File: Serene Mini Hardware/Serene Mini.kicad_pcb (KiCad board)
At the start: 6 copper layers, 35 x 60.5 mm, 52 parts, among them J1 USB_C_Receptacle, J2 Conn_01x04_Pin, U1 AP7361C-33E, U2 AP2112K-1.8, U3 STM32H753ZITx, U4 ADXL382-1BCCZ-RL, U5 ADAU1787BCBZRL, Y1 Crystal_GND24, Y2 32.768 kHz

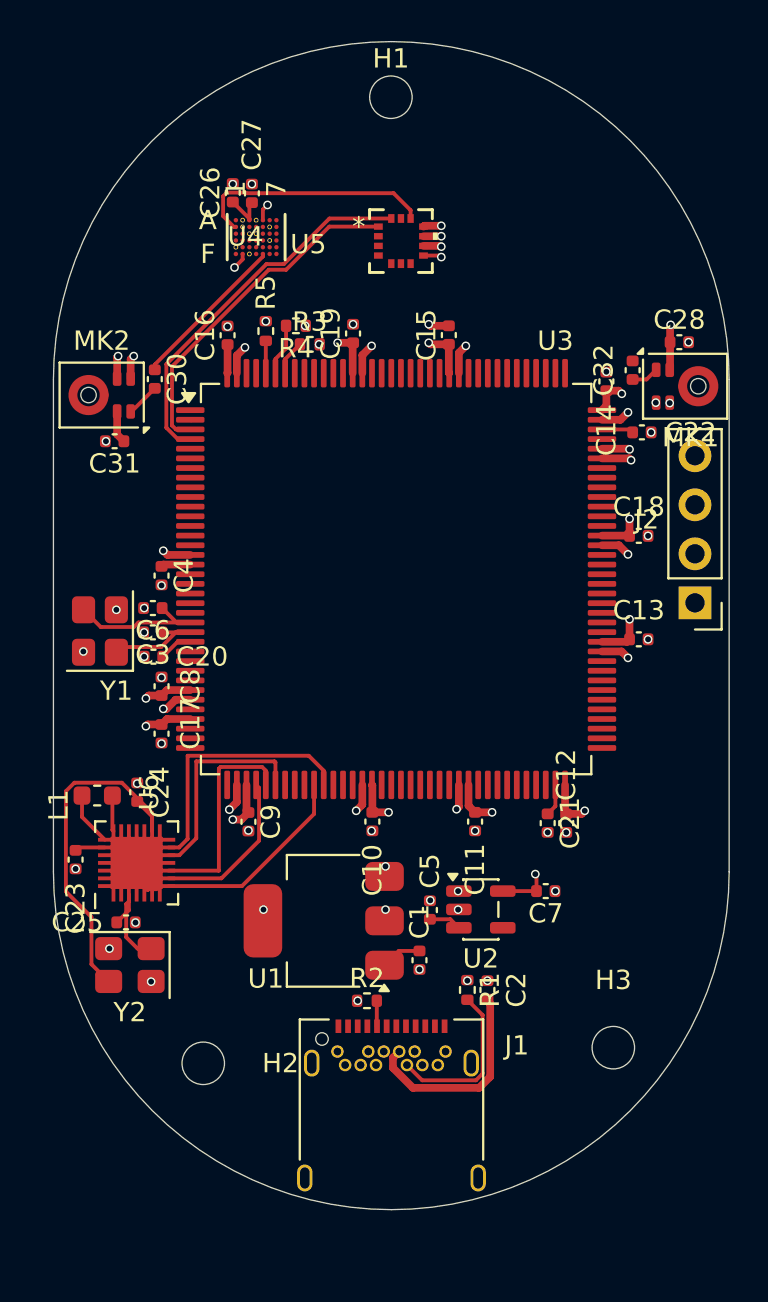
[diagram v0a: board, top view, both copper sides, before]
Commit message: PCB and Schematic Design Changes
Upgraded to the newer sr1120
Reduced the PCB size by ~40%
More efficient layout with chips on both side of the pcb
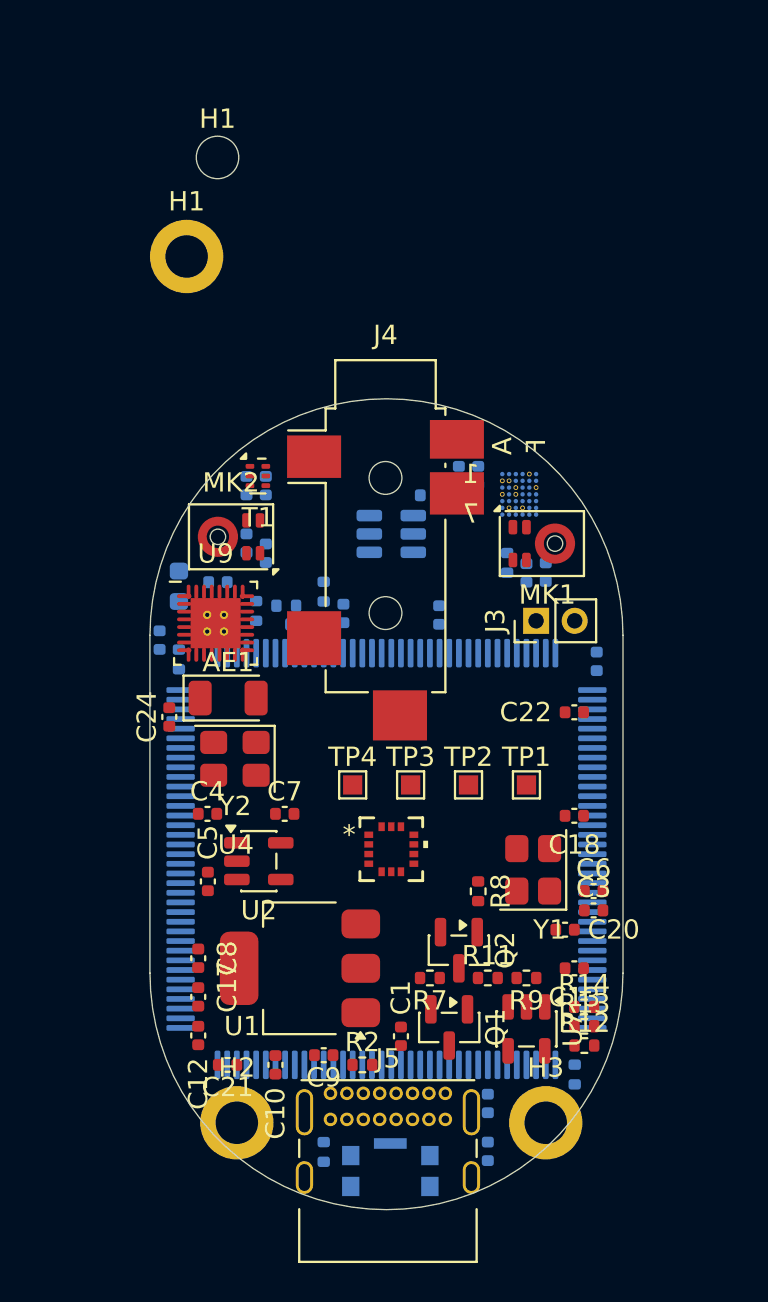
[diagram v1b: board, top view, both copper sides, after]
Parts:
- removed the H1 at (33.5, 20.9)
- removed J1: USB_C_Receptacle, Connector_USB:USB_C_Receptacle_Amphenol_12401548E4-2A
- removed J2: Conn_01x04_Pin, Connector_PinHeader_2.54mm:PinHeader_1x04_P2.54mm_Vertical
- removed U6: ~, ANC_Parts:Spark_SR1020_QFN28
- added AE1: Antenna_Chip, RF_Antenna:Johanson_2450AT18x100, F.Cu at (25.1, 52.0)
- added C29: 1uF, Capacitor_SMD:C_0402_1005Metric, B.Cu at (35.5, 41.5)
- added C33: 10pF, Capacitor_SMD:C_0402_1005Metric, B.Cu at (26.0, 41.0)
- added C34: 10pF, Capacitor_SMD:C_0402_1005Metric, B.Cu at (27.0, 41.0)
- added H1: MountingHole, MountingHole:MountingHole_2.2mm_M2_DIN965_Pad, F.Cu at (22.9, 29.1)
- added H1: MountingHole, MountingHole:MountingHole_2.2mm_M2, F.Cu at (24.5, 24.0)
- added J3: Conn_01x02, Connector_PinHeader_2.00mm:PinHeader_1x02_P2.00mm_Vertical, F.Cu at (41.0, 48.0)
- added J4: AudioJack3_Switch, Connector_Audio:Jack_3.5mm_CUI_SJ2-3593D-SMT_Horizontal, F.Cu at (33.2, 43.1)
- added J5: USB_C_Receptacle_USB2.0_14P, Connector_USB:USB_C_Receptacle_GCT_USB4085, F.Cu at (30.4, 72.5)
- added Q1: Q_PMOS_GSD, Package_TO_SOT_SMD:SOT-23, F.Cu at (36.5, 69.1)
- added Q2: Q_NPN_BCE, Package_TO_SOT_SMD:SOT-23, F.Cu at (37.0, 65.1)
- added R10: 100kΩ, Resistor_SMD:R_0402_1005Metric, B.Cu at (39.5, 45.0)
- added R11: 100kΩ, Resistor_SMD:R_0402_1005Metric, F.Cu at (38.5, 66.5)
- added R12: 220Ω, Resistor_SMD:R_0402_1005Metric, F.Cu at (43.5, 70.0)
- added R13: 100Ω, Resistor_SMD:R_0402_1005Metric, F.Cu at (43.5, 69.0)
- added R14: 100Ω, Resistor_SMD:R_0402_1005Metric, F.Cu at (43.5, 68.0)
- added R15: 10kΩ, Resistor_SMD:R_0402_1005Metric, B.Cu at (30.0, 46.5)
- added R16: 100kΩ, Resistor_SMD:R_0402_1005Metric, B.Cu at (22.5, 50.0)
- added R6: 2kΩ, Resistor_SMD:R_0402_1005Metric, B.Cu at (43.0, 71.5)
- added R7: 100kΩ, Resistor_SMD:R_0402_1005Metric, F.Cu at (35.5, 66.5)
- added R8: 10kΩ, Resistor_SMD:R_0402_1005Metric, F.Cu at (38.0, 62.0)
- added R9: 100kΩ, Resistor_SMD:R_0402_1005Metric, F.Cu at (40.5, 66.5)
- added SW1: SW_Push, Button_Switch_SMD:SW_Push_1P1T-SH_NO_CK_KMR2xxG, B.Cu at (33.5, 76.5)
- added T1: Transformer_1P_1S, RF_Converter:Balun_Johanson_1.6x0.8mm, F.Cu at (26.6, 40.5)
- added TP1: TestPoint, TestPoint:TestPoint_Pad_1.0x1.0mm, F.Cu at (40.5, 56.5)
- added TP2: TestPoint, TestPoint:TestPoint_Pad_1.0x1.0mm, F.Cu at (37.5, 56.5)
- added TP3: TestPoint, TestPoint:TestPoint_Pad_1.0x1.0mm, F.Cu at (34.5, 56.5)
- added TP4: TestPoint, TestPoint:TestPoint_Pad_1.0x1.0mm, F.Cu at (31.5, 56.5)
- added U7: MCP73831-2-OT, Package_TO_SOT_SMD:SOT-23-5, F.Cu at (40.5, 69.1)
- added U8: USBLC6-2SC6, Package_TO_SOT_SMD:SOT-23-6, B.Cu at (33.5, 43.5)
- added U9: ~, ANC_Parts:Spark_SR1120_QFN32, F.Cu at (24.4, 48.1)
- C11, C14, C15, C16, C19, C2, C23, C25, C26, C27, C28, C30, C31, C32, L1, R1, R3, R4, R5, U3, U5: moved to B.Cu
- H2, H3: footprint MountingHole:MountingHole_2.2mm_M2 -> MountingHole:MountingHole_2.2mm_M2_DIN965_Pad
- moved U4 31.5 mm to (33.5, 59.8)
- moved C6 27.1 mm to (44.0, 62.0), turned to 0 degrees
- moved C3 27.0 mm to (44.0, 63.0), turned to 0 degrees
- moved Y1 25.6 mm to (40.9, 60.9)
- moved C20 25.6 mm to (42.5, 64.0)
- moved C12 22.0 mm to (23.5, 69.5), turned to 90 degrees
- moved C21 20.8 mm to (25.0, 71.0), turned to 180 degrees
- moved C26 19.4 mm to (38.0, 40.5), turned to -90 degrees
- moved U5 19.1 mm to (40.1, 41.5), turned to -90 degrees
- moved C25 18.3 mm to (24.5, 46.0)
- moved C27 18.1 mm to (37.0, 40.5), turned to -90 degrees
- moved C13 17.4 mm to (43.0, 66.0), turned to 180 degrees
- moved C11 17.1 mm to (38.5, 75.5)
- moved C22 14.9 mm to (43.0, 52.7), turned to 180 degrees
- moved C18 14.9 mm to (43.0, 58.1), turned to 180 degrees
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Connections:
- C23 pad 1: Net-(U6-AVDD_1V) -> Net-(U9-VDD_IO)
- L1 pad 1: Net-(U6-AVDD_1V) -> Net-(U9-VDD_CORE_ANA)
- U3 pad 115: unconnected-(U3-PD1-Pad115) -> /HP_DETECT
- U3 pad 133: unconnected-(U3-PB3-Pad133) -> /UWB_SHDN
- U3 pad 34: unconnected-(U3-PA0-Pad34) -> /<NO NET>
- U3 pad 35: unconnected-(U3-PA1-Pad35) -> /CHG_STAT
- U3 pad 81: unconnected-(U3-PD12-Pad81) -> /PWR_HOLD
- U3 pad 82: unconnected-(U3-PD13-Pad82) -> /LED_R
- U3 pad 85: unconnected-(U3-PD14-Pad85) -> /LED_G
- U3 pad 86: unconnected-(U3-PD15-Pad86) -> /LED_B
- U5 pad E1: GND -> +1V8
- U5 pad E2: unconnected-(U5-HPOUTP0/LOUTP0-PadE2) -> /HPOUTR
- U5 pad F1: unconnected-(U5-HPOUTN0/LOUTP0-PadF1) -> /HPOUTL
- U5 pad F2: +1V8 -> +3.3V
- U5 pad F4: unconnected-(U5-CM-PadF4) -> +1V8
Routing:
- net +3.3V: track 49.9 -> 0.00 mm, vias 21 -> 0
- net GND: track 21.2 -> 0.00 mm, vias 53 -> 0
- net Net-(U9-XTAL_C2): track 19.6 -> 0.00 mm
- net /SAI_BCLK: track 19.5 -> 0.00 mm
- net /SAI_FS: track 17.8 -> 0.00 mm
- net /UWB_RST: track 13.6 -> 0.00 mm
- net /VIB_DATA: track 12.5 -> 0.00 mm
- net /UWB_SCK: track 11.2 -> 0.00 mm
- net /UWB_MISO: track 11.1 -> 0.00 mm
- net /UWB_IRQ: track 10.6 -> 0.00 mm
- net Net-(J5-CC2): track 8.54 -> 0.00 mm
- net /UWB_CS: track 8.45 -> 0.00 mm
- net /MIC2: track 8.32 -> 0.00 mm
- net Net-(U3-PH0): track 7.76 -> 0.00 mm
- net Net-(U3-PH1): track 5.72 -> 0.00 mm
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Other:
- board size 35 x 60.5 mm -> 24.5 x 42 mm

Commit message: Final PCB and Schematic Design
- Added new IC to support fast charging for batteries up to 3000mAh

- Added a bluetooth chip

- Used smaller coaxial ports to increase available space

- The button is now located off the board connected via molax

- Finished routing
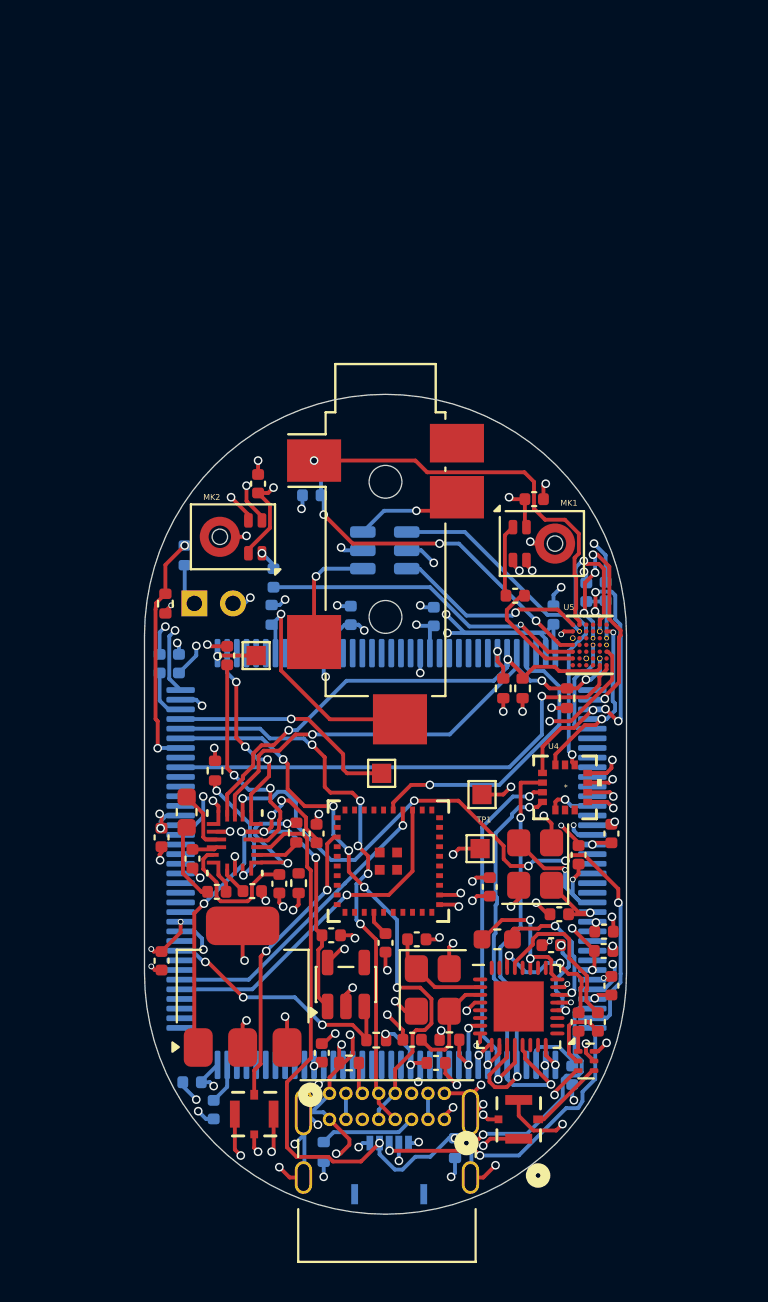
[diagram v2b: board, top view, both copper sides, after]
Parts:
- removed AE1: Antenna_Chip, RF_Antenna:Johanson_2450AT18x100
- removed C5: 10uF, Capacitor_SMD:C_0402_1005Metric
- removed H1, H2, H3: MountingHole, MountingHole:MountingHole_2.2mm_M2_DIN965_Pad
- removed H1: MountingHole, MountingHole:MountingHole_2.2mm_M2
- removed Q1: Q_PMOS_GSD, Package_TO_SOT_SMD:SOT-23
- removed Q2: Q_NPN_BCE, Package_TO_SOT_SMD:SOT-23
- removed R13, R14: 100Ω, Resistor_SMD:R_0402_1005Metric
- removed SW1: SW_Push, Button_Switch_SMD:SW_Push_1P1T-SH_NO_CK_KMR2xxG
- added C35: 4.7µF, Capacitor_SMD:C_0402_1005Metric, F.Cu at (26.3, 62.0)
- added C36: 10uF, Capacitor_SMD:C_0402_1005Metric, F.Cu at (30.4, 64.3)
- added C37: 47nF, Capacitor_SMD:C_0402_1005Metric, F.Cu at (24.5, 62.0)
- added C38: 10uF, Capacitor_SMD:C_0402_1005Metric, F.Cu at (29.6, 59.0)
- added C39: 10uF, Capacitor_SMD:C_0402_1005Metric, F.Cu at (23.2, 60.3)
- added C40: 10uF, Capacitor_SMD:C_0402_1005Metric, F.Cu at (27.7, 61.6)
- added J1: Conn_Coaxial, ANC_Parts:CONN_X.FL-R-SMT-180_HIR, F.Cu at (40.1, 73.8)
- added J2: Conn_01x06_Socket, ANC_Parts:CONN_503480-0540_MOL, B.Cu at (33.4, 76.6)
- added J6: Conn_Coaxial, ANC_Parts:CONN_X.FL-R-SMT-180_HIR, F.Cu at (26.4, 73.6)
- added L2: 1.5uH, Inductor_SMD:L_0603_1608Metric, F.Cu at (22.9, 57.9)
- added U6: BQ25620RYKR, ANC_Parts:WQFN-HR18__RYK_TEX, F.Cu at (25.4, 59.5)
- C11, C2, C23, C25, C28, C31, C32, C33, C34, L1, R10, R16, R3, R4, R5, U5: moved to F.Cu
- C12, C21, C22, C9, J3, R9: moved to B.Cu
- R11: value 100kΩ -> 10kΩ; moved to B.Cu
- R12: value 220Ω -> 100kΩ
- R6: value 2kΩ -> 160Ω; moved to F.Cu
- R7: value 100kΩ -> 10kΩ
- U7: value MCP73831-2-OT -> BGM220SC12WGA2R; footprint Package_TO_SOT_SMD:SOT-23-5 -> ANC_Parts:BGM220S_SIL
- moved T1 34.7 mm to (43.6, 70.8)
- moved C33 33.2 mm to (44.2, 68.8)
- moved C34 32.2 mm to (43.2, 68.8), turned to -90 degrees
- moved R9 28.2 mm to (22.8, 44.6), turned to -90 degrees
- moved C23 25.7 mm to (41.8, 64.8), turned to 180 degrees
- moved U9 25.3 mm to (40.1, 68.0)
- moved L1 24.6 mm to (39.0, 64.5), turned to 0 degrees
- moved R6 24.4 mm to (24.4, 55.8), turned to 90 degrees
- moved R16 24.2 mm to (36.5, 69.7), turned to 0 degrees
- moved C1 21.7 mm to (25.0, 49.8)
- moved C14 21.6 mm to (22.5, 50.2)
- moved C22 21.6 mm to (21.5, 50.2), turned to 90 degrees
- moved C18 21.4 mm to (21.6, 59.2), turned to -90 degrees
- moved C17 21.4 mm to (44.9, 66.9), turned to 90 degrees
- moved C13 21.4 mm to (21.6, 65.6), turned to -90 degrees
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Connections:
- C1 pad 1: Net-(U1-VI) -> GND
- C1 pad 2: +5V -> Net-(J3-Pin_1)
- C2 pad 2: +3.3V -> Net-(U7-DECOUPLE)
- C29 pad 1: +1V8 -> /CM
- J4 pad S: +1V8 -> /CM
- J5 pad A4: +5V -> Net-(U6-VBUS)
- J5 pad A6: unconnected-(J5-D+-PadA6) -> /USB_DM
- J5 pad A7: unconnected-(J5-D--PadA7) -> /USB_DP
- J5 pad A9: +5V -> Net-(U6-VBUS)
- J5 pad B4: +5V -> Net-(U6-VBUS)
- J5 pad B6: +3.3V -> /USB_DM
- J5 pad B7: +3.3V -> /USB_DP
- J5 pad B9: +5V -> Net-(U6-VBUS)
- R10 pad 1: /<NO NET> -> /BATT_SENSE
- R11 pad 1: Net-(Q1-G) -> /BTN_SENSE
- R11 pad 2: /<NO NET> -> +3.3V
- R12 pad 1: /LED_R -> /V1P8_EN
- R12 pad 2: Net-(D1-R) -> GND
- R6 pad 1: Net-(U7-PROG) -> Net-(U6-ILIM)
- R7 pad 1: Net-(J3-Pin_1) -> Net-(U6-TS_BIAS)
- R7 pad 2: Net-(Q1-G) -> Net-(U6-TS)
- R8 pad 1: /PWR_HOLD -> Net-(U6-TS)
- R8 pad 2: Net-(Q2-B) -> GND
- R9 pad 1: /<NO NET> -> /BATT_SENSE
- T1 pad 5: (no net) -> GND
- T1 pad 6: (no net) -> GND
- U1 pad 1: Net-(U1-VI) -> +5V
- U2 pad 1: +3.3V -> +5V
- U2 pad 3: Net-(U2-EN) -> /V1P8_EN
- U3 pad 102: unconnected-(U3-PA10-Pad102) -> /BATT_SENSE
- U3 pad 103: +3.3V -> /USB_DP
- U3 pad 104: +3.3V -> /USB_DM
- U3 pad 110: unconnected-(U3-PA15-Pad110) -> /CHG_STAT
- U3 pad 13: unconnected-(U3-PF3-Pad13) -> /ACC_CS
- U3 pad 133: /UWB_SHDN -> unconnected-(U3-PB3-Pad133)
- U3 pad 141: unconnected-(U3-PE0-Pad141) -> /BLT_RESET
- U3 pad 26: /ACC_CS -> unconnected-(U3-PC0-Pad26)
- U3 pad 34: /<NO NET> -> /BTN_SENSE
- U3 pad 35: /CHG_STAT -> /CHG_INT
- U3 pad 36: unconnected-(U3-PA2-Pad36) -> /LED_DATA
- U3 pad 37: unconnected-(U3-PA3-Pad37) -> /UWB_RST
- U3 pad 40: /UWB_CS -> unconnected-(U3-PA4-Pad40)
- U3 pad 44: unconnected-(U3-PC4-Pad44) -> /UWB_CS
- U3 pad 45: unconnected-(U3-PC5-Pad45) -> /UWB_IRQ
- U3 pad 46: /UWB_IRQ -> /UWB_SHDN
- U3 pad 47: /UWB_RST -> unconnected-(U3-PB1-Pad47)
- U3 pad 77: unconnected-(U3-PD8-Pad77) -> /RX
- U3 pad 78: unconnected-(U3-PD9-Pad78) -> /TX
- U3 pad 81: /PWR_HOLD -> /V1P8_EN
- U5 pad E1: +1V8 -> /CM
- U5 pad F2: +3.3V -> +1V8
- U5 pad F4: +1V8 -> /CM
- U7 pad 1: /CHG_STAT -> unconnected-(U7-NC-Pad1)
- U7 pad 2: GND -> unconnected-(U7-ANT_IN-Pad2)
- U7 pad 3: Net-(J3-Pin_1) -> Net-(J6-In)
- U7 pad 4: +5V -> unconnected-(U7-GND-Pad4)
- U7 pad 5: Net-(U7-PROG) -> unconnected-(U7-GND-Pad5)
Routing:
- net GND: track 0.00 -> 111.7 mm, vias 0 -> 91
- net +3.3V: track 0.00 -> 64.5 mm, vias 0 -> 35
- net +1V8: track 0.00 -> 48.3 mm, vias 0 -> 6
- net /BTN_SENSE: track 0.00 -> 43.5 mm, vias 0 -> 3
- net /CM: track 0.00 -> 39.6 mm, vias 0 -> 4
- net /CHG_INT: track 0.00 -> 34.5 mm, vias 0 -> 5
- net +5V: track 0.00 -> 33.2 mm, vias 0 -> 6
- net /USB_DP: track 0.00 -> 30.6 mm, vias 0 -> 5
- net /USB_DM: track 0.00 -> 29.7 mm, vias 0 -> 5
- net /SYS_MCLK: track 0.00 -> 25.8 mm, vias 0 -> 1
- net /I2C_SDA: track 0.00 -> 25.4 mm, vias 0 -> 3
- net /I2C_SCL: track 0.00 -> 25.4 mm, vias 0 -> 2
- net /UWB_MISO: track 0.00 -> 21.1 mm, vias 0 -> 2
- net /UWB_SCK: track 0.00 -> 20.6 mm, vias 0 -> 2
- net /UWB_MOSI: track 0.00 -> 19.5 mm, vias 0 -> 2
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- added copper zone on In4.Cu, net +3.3V
- added copper zone on In1.Cu, net GND
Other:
- board size 24.5 x 42 mm -> 25 x 42.5 mm

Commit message: PCB Fixes
Connected some missing traces and fixed some clearance issues
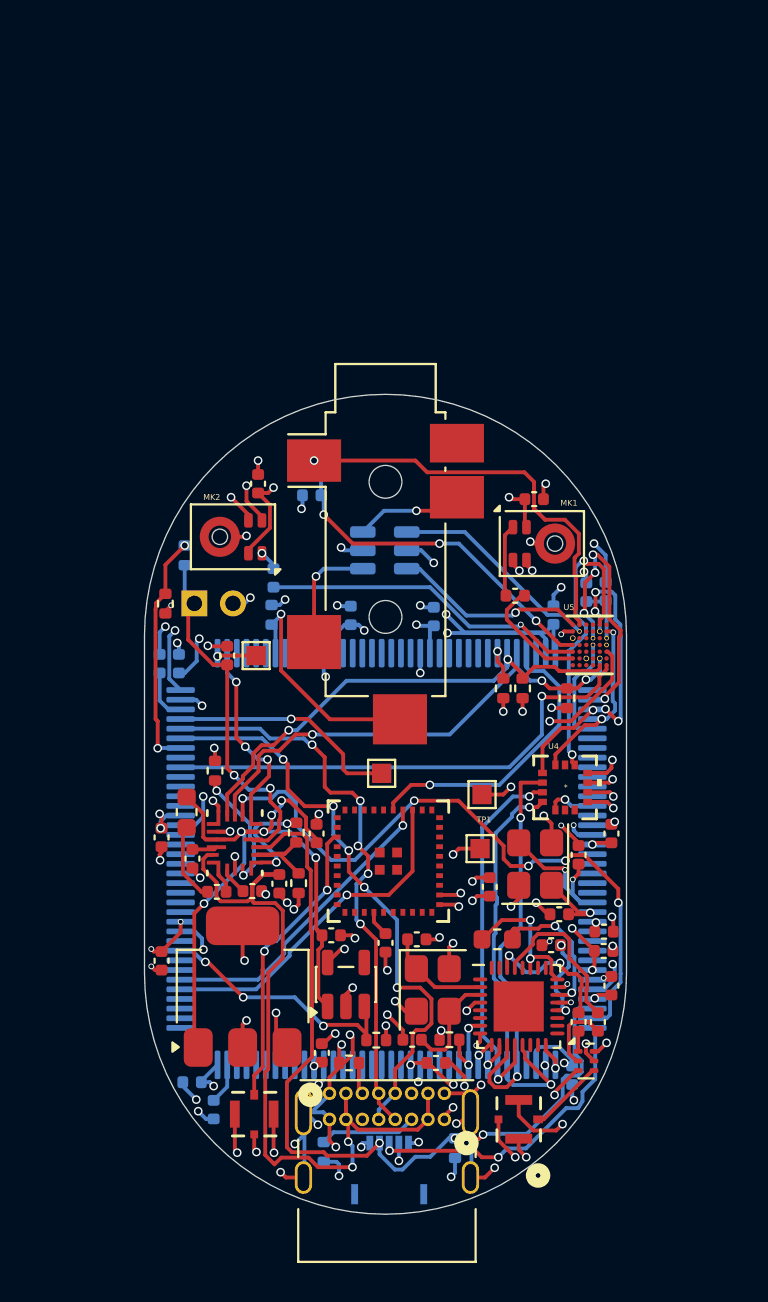
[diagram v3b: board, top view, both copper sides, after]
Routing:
- net Net-(U6-VBUS): track 9.81 -> 40.0 mm, vias 0 -> 2
- net Net-(J3-Pin_1): track 13.5 -> 18.1 mm
- net Net-(U6-TS): track 2.35 -> 4.88 mm
- net +5V: track 33.2 -> 35.3 mm
- net Net-(U6-TS_BIAS): track 6.31 -> 5.26 mm
- net +3.3V: track 64.5 -> 65.4 mm, vias 35 -> 36
- net GND: track 111.7 -> 112.0 mm, vias 91 -> 92
